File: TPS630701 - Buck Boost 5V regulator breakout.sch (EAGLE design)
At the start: 17 parts, among them IC1 TPS630701RNMT

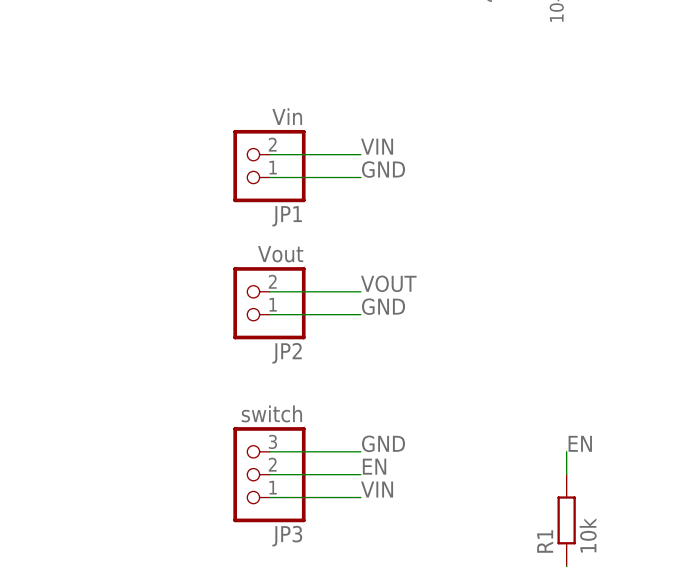
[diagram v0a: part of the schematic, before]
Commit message: - recreated gerbers with better layer names & corrected mission dimension layer
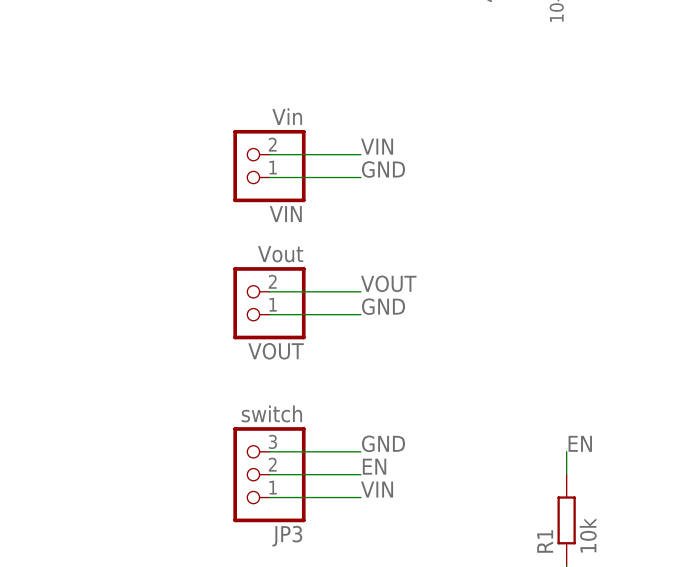
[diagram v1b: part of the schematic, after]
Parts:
- renumbered JP1 to VIN, JP2 to VOUT
